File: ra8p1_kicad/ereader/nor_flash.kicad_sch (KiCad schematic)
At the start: 5 parts, among them U15 S28HL01GTFPBHI030

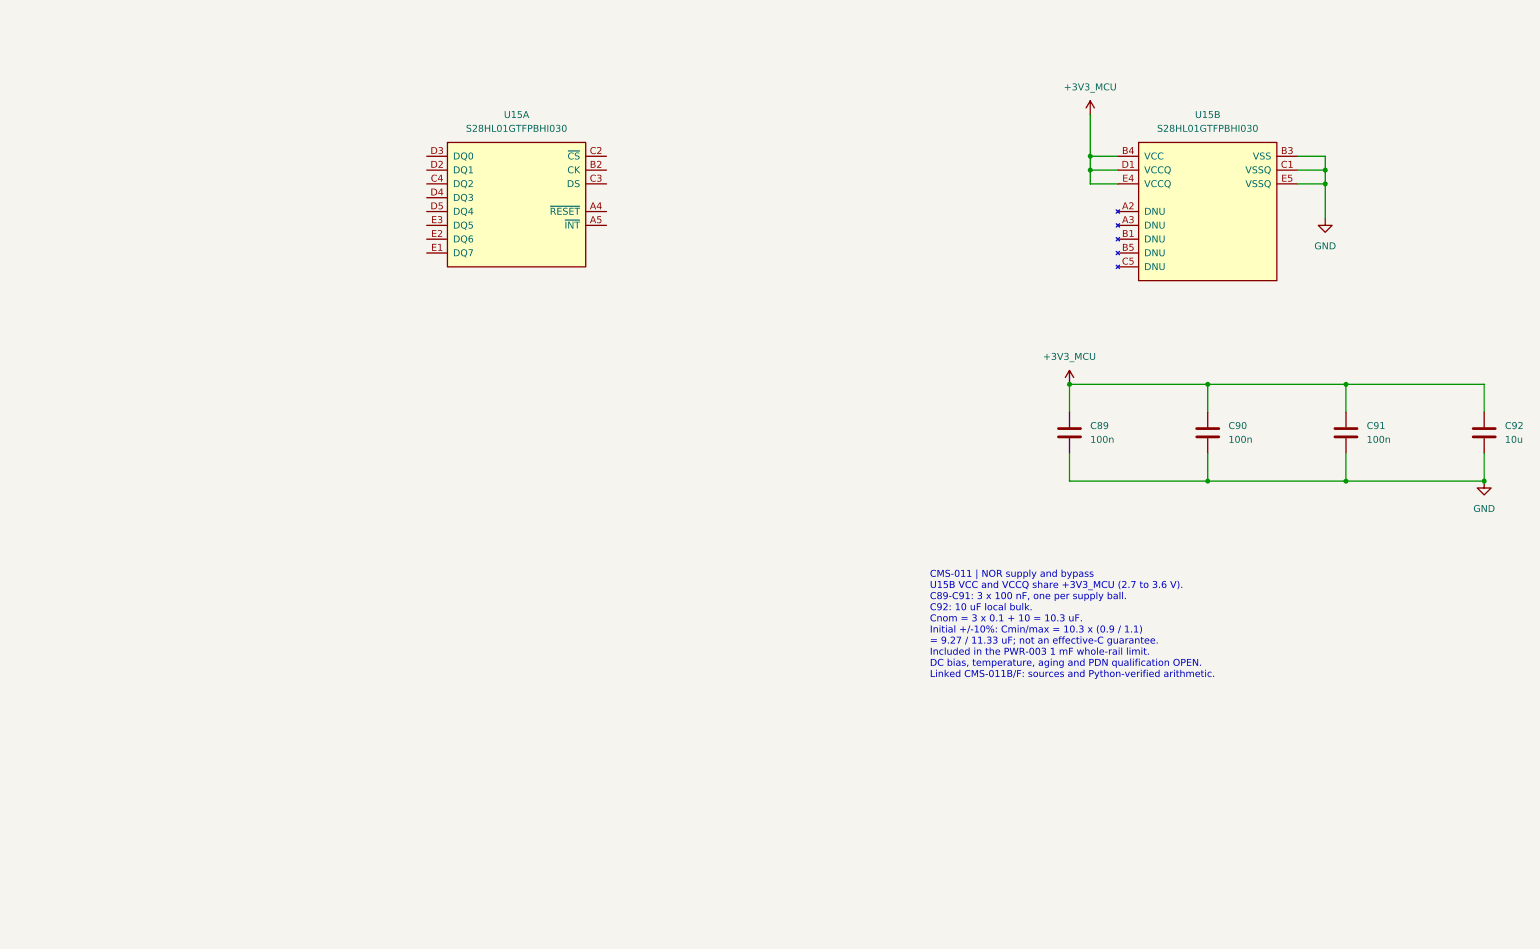
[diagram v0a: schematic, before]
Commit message: Add sourced Octal NOR series and default-state network
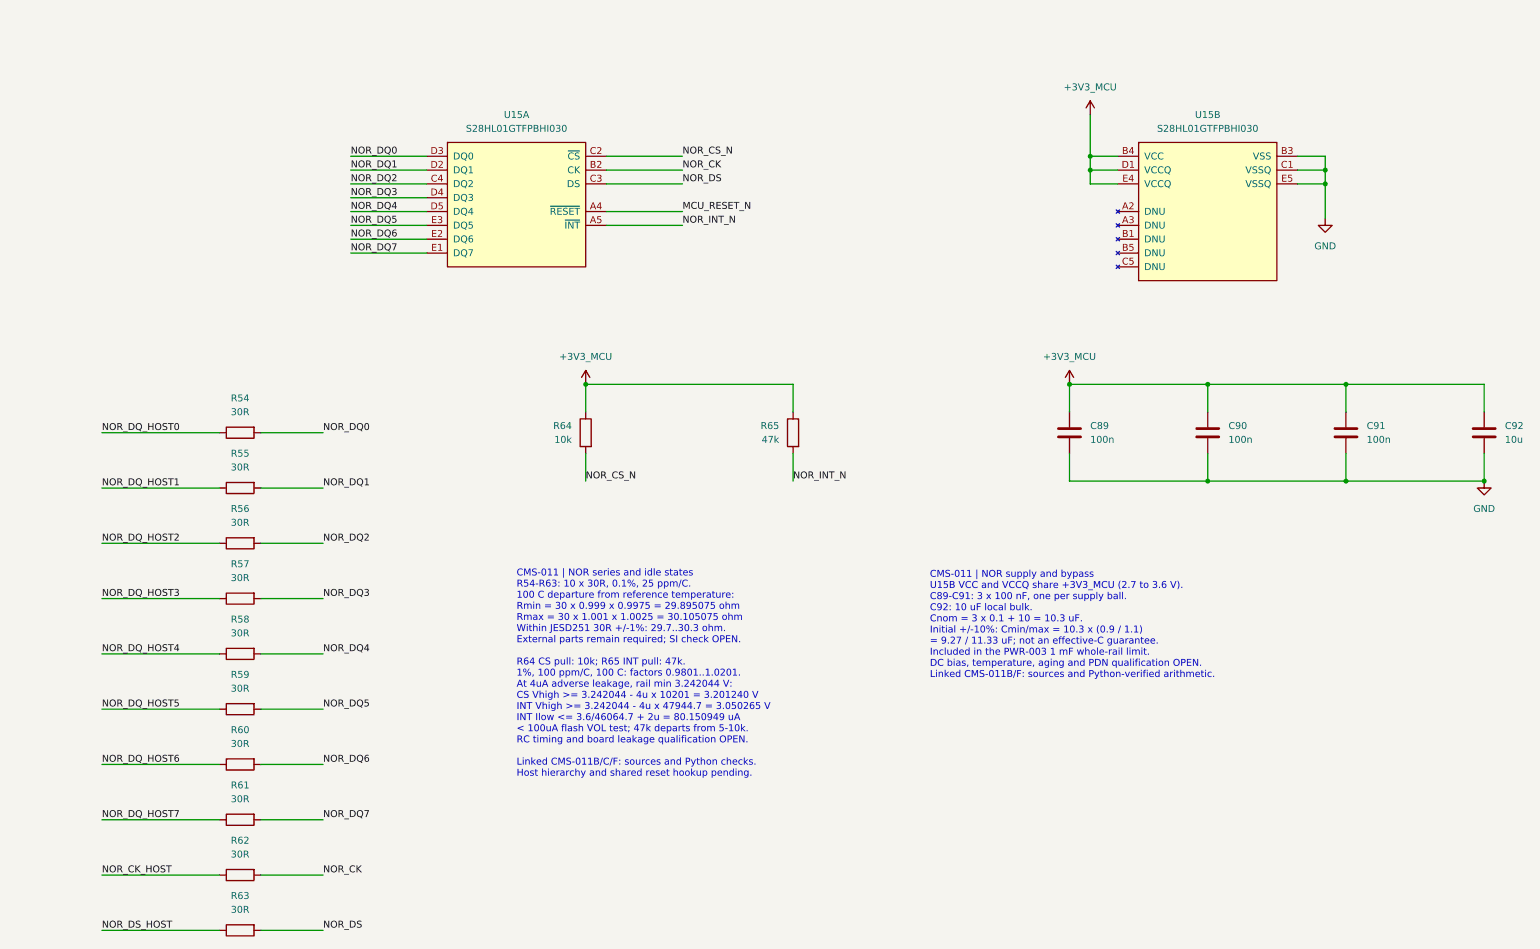
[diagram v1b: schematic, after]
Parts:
- added R54, R55, R56, R57, R58, R59, R60, R61, R62, R63: 30R, symbol Device:R
- added R64: 10k, symbol Device:R
- added R65: 47k, symbol Device:R
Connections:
- net +3V3_MCU: now also R64.1, R65.1
- net MCU_RESET_N: now reaches U15.A4 (~{RESET})
- net NOR_INT_N: now reaches U15.A5 (~{INT})
- net NOR_INT_N: now also R65.2
- net NOR_CK: now reaches U15.B2 (CK)
- net NOR_CK: now also R62.2
- net NOR_CS_N: now reaches U15.C2 (~{CS})
- net NOR_CS_N: now also R64.2
- net NOR_DS: now reaches U15.C3 (DS)
- net NOR_DS: now also R63.2
- net NOR_DQ2: now reaches U15.C4 (DQ2)
- net NOR_DQ2: now also R56.2
- net NOR_DQ1: now reaches U15.D2 (DQ1)
- net NOR_DQ1: now also R55.2
- net NOR_DQ0: now reaches U15.D3 (DQ0)
- net NOR_DQ0: now also R54.2
- net NOR_DQ3: now reaches U15.D4 (DQ3)
- net NOR_DQ3: now also R57.2
- net NOR_DQ4: now reaches U15.D5 (DQ4)
- net NOR_DQ4: now also R58.2
- net NOR_DQ7: now reaches U15.E1 (DQ7)
- net NOR_DQ7: now also R61.2
- net NOR_DQ6: now reaches U15.E2 (DQ6)
- net NOR_DQ6: now also R60.2
- net NOR_DQ5: now reaches U15.E3 (DQ5)
- net NOR_DQ5: now also R59.2
- new net NOR_CK_HOST: R62.1
- new net NOR_DQ_HOST0: R54.1
- new net NOR_DQ_HOST1: R55.1
- new net NOR_DQ_HOST2: R56.1
- new net NOR_DQ_HOST3: R57.1
- new net NOR_DQ_HOST4: R58.1
- new net NOR_DQ_HOST5: R59.1
- new net NOR_DQ_HOST6: R60.1
- new net NOR_DQ_HOST7: R61.1
- new net NOR_DS_HOST: R63.1
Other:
- note added: "CMS-011 | NOR series and idle states R54-R63: 10 x 30R, 0.1%, 25 ppm/C. 100 C departure from reference temperature: Rmin = 30 x 0.999 x 0.9975 = 29.895075 ohm Rmax = 30 x 1.001 x 1.0025 = 30.105075 ohm Within JESD251 30R +/-1%: 29.7..30.3 ohm. External parts remain required; SI check OPEN. R64 CS pull: 10k; R65 INT pull: 47k. 1%, 100 ppm/C, 100 C: factors 0.9801..1.0201. At 4uA adverse leakage, r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"

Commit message: Connect Octal NOR hierarchy and configured MCU pins
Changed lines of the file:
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@@
 		(rev "0.3 DRAFT")
 	)
-	(text "CMS-011 | NOR series and idle states\nR54-R63: 10 x 30R, 0.1%, 25 ppm/C.\n100 C departure from reference temperature:\nRmin = 30 x 0.999 x 0.9975 = 29.895075 ohm\nRmax = 30 x 1.001 x 1.0025 = 30.105075 ohm\nWithin JESD251 30R +/-1%: 29.7..30.3 ohm.\nExternal parts remain required; SI check OPEN.\n\nR64 CS pull: 10k; R65 INT pull: 47k.\n1%, 100 ppm/C, 100 C: factors 0.9801..1.0201.\nAt 4uA adverse leakage, rail min 3.242044 V:\nCS Vhigh >= 3.242044 - 4u x 10201 = 3.201240 V\nINT Vhigh >= 3.242044 - 4u x 47944.7 = 3.050265 V\nINT Ilow <= 3.6/46064.7 + 2u = 80.150949 uA\n< 100uA flash VOL test; 47k departs from 5-10k.\nRC timing and board leakage qualification OPEN.\n\nLinked CMS-011B/C/F: sources and Python checks.\nHost hierarchy and shared reset hookup pending."
+	(text "CMS-011 | NOR series and idle states\nR54-R63: 10 x 30R, 0.1%, 25 ppm/C.\n100 C departure from reference temperature:\nRmin = 30 x 0.999 x 0.9975 = 29.895075 ohm\nRmax = 30 x 1.001 x 1.0025 = 30.105075 ohm\nWithin JESD251 30R +/-1%: 29.7..30.3 ohm.\nExternal parts remain required; SI check OPEN.\n\nR64 CS pull: 10k; R65 INT pull: 47k.\n1%, 100 ppm/C, 100 C: factors 0.9801..1.0201.\nAt 4uA adverse leakage, rail min 3.242044 V:\nCS Vhigh >= 3.242044 - 4u x 10201 = 3.201240 V\nINT Vhigh >= 3.242044 - 4u x 47944.7 = 3.050265 V\nINT Ilow <= 3.6/46064.7 + 2u = 80.150949 uA\n< 100uA flash VOL test; 47k departs from 5-10k.\nRC timing and board leakage qualification OPEN.\n\nLinked CMS-011B/C/F: sources and Python checks.\nMCU hierarchy and common reset connected.\nDS is read-only: P801 input, WRMSKMD=0.\nCMS-011D defines reset and protocol recovery."
 		(exclude_from_sim no)
 		(at 152.4 164.846 0)
@@
 		)
 	)
+	(bus
+		(pts
+			(xy 63.5 63.5) (xy 76.2 63.5)
+		)
+		(stroke
+			(width 0)
+			(type default)
+		)
+	)
 	(wire
 		(pts
@@
 	(wire
 		(pts
+			(xy 168.91 99.06) (xy 182.88 99.06)
+		)
+		(stroke
+			(width 0)
+			(type default)
+		)
+	)
+	(wire
+		(pts
 			(xy 121.92 91.44) (xy 135.89 91.44)
 		)
@@
 		(pts
 			(xy 254 148.59) (xy 279.4 148.59)
-		)
-		(stroke
-			(width 0)
-			(type default)
-		)
-	)
-	(wire
-		(pts
-			(xy 168.91 99.06) (xy 182.88 99.06)
 		)
 		(stroke
@@
 		)
 	)
-	(label "NOR_CS_N"
-		(at 165.1 148.59 0)
-		(effects
-			(font
-				(size 1.27 1.27)
-			)
-			(justify left bottom)
-		)
-	)
 	(label "NOR_DQ_HOST6"
 		(at 76.2 200.66 0)
@@
 		)
 	)
-	(label "NOR_CK_HOST"
-		(at 76.2 220.98 0)
-		(effects
-			(font
-				(size 1.27 1.27)
-			)
-			(justify left bottom)
-		)
-	)
 	(label "NOR_DQ0"
 		(at 121.92 88.9 0)
@@
 		)
 	)
-	(label "NOR_DS_HOST"
-		(at 76.2 231.14 0)
-		(effects
-			(font
-				(size 1.27 1.27)
-			)
-			(justify left bottom)
-		)
-	)
 	(label "NOR_DQ0"
 		(at 116.84 139.7 0)
@@
 		)
 	)
-	(label "NOR_INT_N"
-		(at 203.2 148.59 0)
-		(effects
-			(font
-				(size 1.27 1.27)
-			)
-			(justify left bottom)
-		)
-	)
 	(label "NOR_DQ5"
 		(at 121.92 101.6 0)
@@
 		)
 	)
-	(label "MCU_RESET_N"
+	(hierarchical_label "NOR_INT_N"
+		(shape output)
+		(at 203.2 148.59 180)
+		(effects
+			(font
+				(size 1.27 1.27)
+			)
+			(justify right)
+		)
+	)
+	(hierarchical_label "MCU_RESET_N"
+		(shape input)
 		(at 182.88 99.06 0)
 		(effects
@@
 				(size 1.27 1.27)
 			)
-			(justify left bottom)
-		)
-	)
+			(justify left)
+		)
+	)
+	(hierarchical_label "NOR_CK_HOST"
+		(shape input)
+		(at 76.2 220.98 180)
+		(effects
+			(font
+				(size 1.27 1.27)
+			)
+			(justify right)
+		)
+	)
+	(hierarchical_label "NOR_DS_HOST"
+		(shape output)
+		(at 76.2 231.14 180)
+		(effects
+			(font
+				(size 1.27 1.27)
+			)
+			(justify right)
+		)
+	)
+	(hierarchical_label "NOR_CS_N"
+		(shape input)
+		(at 165.1 148.59 180)
+		(effects
+			(font
+				(size 1.27 1.27)
+			)
+			(justify right)
+		)
+	)
+	(hierarchical_label "NOR_DQ_HOST[0..7]"
+		(shape bidirectional)
+		(at 76.2 63.5 0)
+		(effects
+			(font
+				(size 1.27 1.27)
+			)
+			(justify left)
+		)
+	)
